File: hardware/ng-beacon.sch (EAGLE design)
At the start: 5 parts

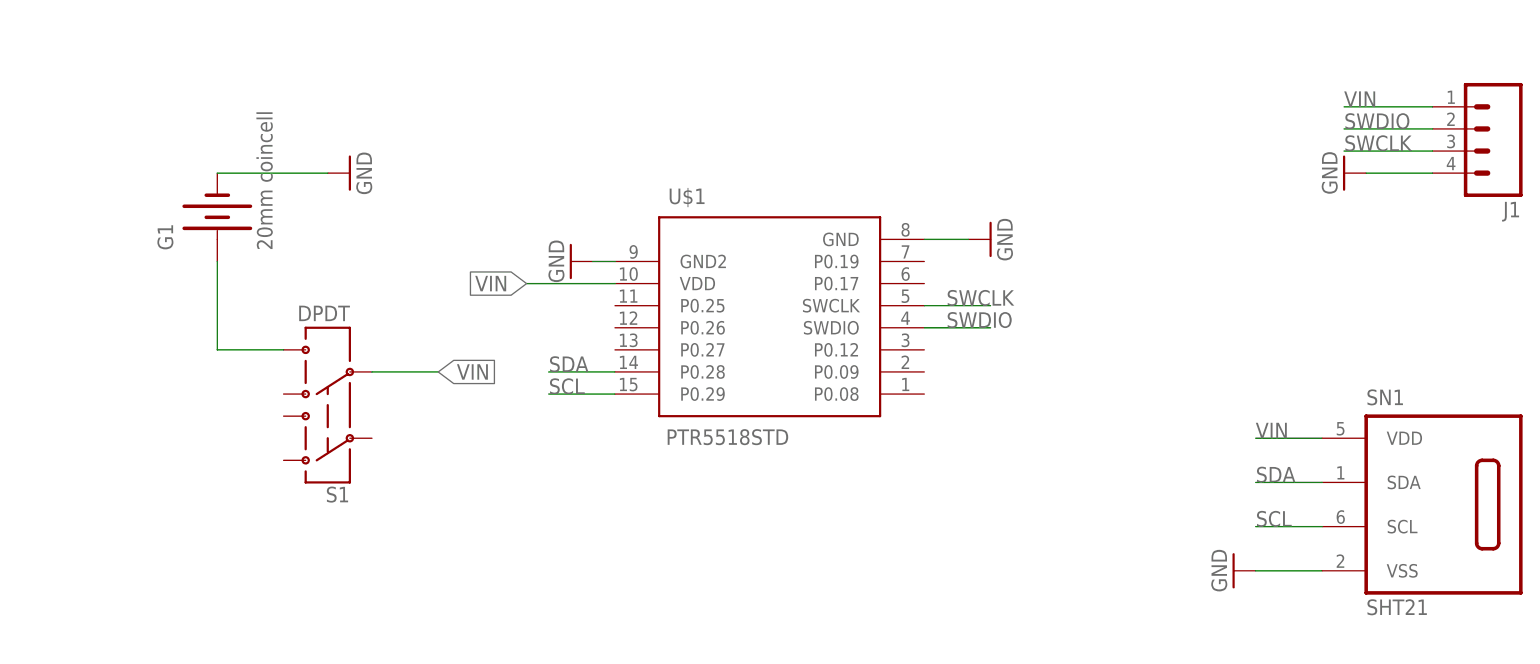
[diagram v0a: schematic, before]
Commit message: refactor: switch to MDBT42 module
nRF52, more pins and smaller footprint
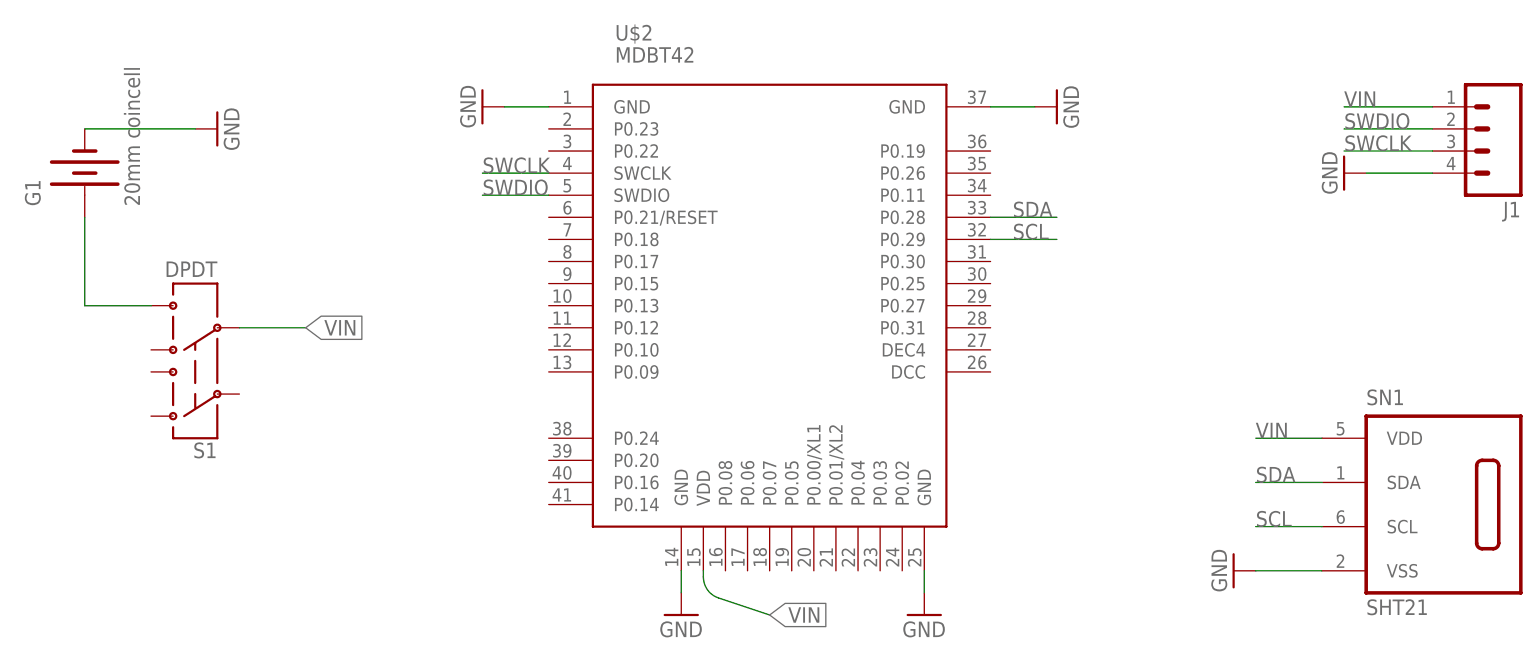
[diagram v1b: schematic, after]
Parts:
- removed U$1: PTR5518STD, PTR5518:PTR5518STD
- added U$2: MDBT42, MDBT42:MDBT42
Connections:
- net GND: now also U$2.GND@1, U$2.GND@14, U$2.GND@25, U$2.GND@37; no longer U$1.GND, U$1.GND2
- net SCL: now also U$2.P0.29; no longer U$1.P0.29
- net SDA: now also U$2.P0.28; no longer U$1.P0.28
- net SWCLK: now also U$2.SWCLK; no longer U$1.SWCLK
- net SWDIO: now also U$2.SWDIO; no longer U$1.SWDIO
- net VIN: now also U$2.VDD; no longer U$1.VDD
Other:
- moved on the sheet: G1, S1
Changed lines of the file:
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@@
 </classes>
 <parts>
-<part name="U$1" library="PTR5518" deviceset="PTR5518" device="STD"/>
 <part name="G1" library="SparkFun-Electromechanical" deviceset="BATTERY" device="20MM_4LEGS" value="20mm coincell"/>
 <part name="S1" library="SparkFun-Electromechanical" deviceset="SWITCH-DPDT" device="AYZ0202" value="DPDT"/>
 <part name="GND1" library="SparkFun-Aesthetics" deviceset="GND" device=""/>
-<part name="GND2" library="SparkFun-Aesthetics" deviceset="GND" device=""/>
 <part name="GND3" library="SparkFun-Aesthetics" deviceset="GND" device=""/>
 <part name="J1" library="SparkFun-Connectors" deviceset="M04" device="LOCK"/>
@@
 <part name="SN1" library="sensirion" deviceset="SHT21" device=""/>
 <part name="GND4" library="SparkFun-Aesthetics" deviceset="GND" device=""/>
+<part name="U$2" library="MDBT42" deviceset="MDBT42" device=""/>
+<part name="GND5" library="SparkFun-Aesthetics" deviceset="GND" device=""/>
+<part name="GND6" library="SparkFun-Aesthetics" deviceset="GND" device=""/>
+<part name="GND7" library="SparkFun-Aesthetics" deviceset="GND" device=""/>
 </parts>
 <sheets>
@@
 </plain>
 <instances>
-<instance part="U$1" gate="G$1" x="30.48" y="58.42"/>
-<instance part="G1" gate="G$1" x="-33.02" y="71.12" rot="R90"/>
-<instance part="S1" gate="G$1" x="-20.32" y="48.26" rot="R180"/>
-<instance part="GND1" gate="1" x="-17.78" y="76.2" rot="R90"/>
-<instance part="GND2" gate="1" x="55.88" y="68.58" rot="R90"/>
-<instance part="GND3" gate="1" x="7.62" y="66.04" rot="R270"/>
+<instance part="G1" gate="G$1" x="-48.26" y="76.2" rot="R90"/>
+<instance part="S1" gate="G$1" x="-35.56" y="53.34" rot="R180"/>
+<instance part="GND1" gate="1" x="-33.02" y="81.28" rot="R90"/>
+<instance part="GND3" gate="1" x="-2.54" y="83.82" rot="R270"/>
 <instance part="J1" gate="G$1" x="111.76" y="81.28" rot="R180"/>
 <instance part="GND8" gate="1" x="96.52" y="76.2" rot="R270"/>
 <instance part="SN1" gate="G$1" x="106.68" y="38.1"/>
 <instance part="GND4" gate="1" x="83.82" y="30.48" rot="R270"/>
+<instance part="U$2" gate="G$1" x="30.48" y="60.96"/>
+<instance part="GND5" gate="1" x="63.5" y="83.82" rot="R90"/>
+<instance part="GND6" gate="1" x="48.26" y="25.4"/>
+<instance part="GND7" gate="1" x="20.32" y="25.4"/>
 </instances>
 <busses>
@@
 <pinref part="GND1" gate="1" pin="GND"/>
 <pinref part="G1" gate="G$1" pin="-"/>
-<wire x1="-33.02" y1="76.2" x2="-20.32" y2="76.2" width="0.1524" layer="91"/>
-</segment>
-<segment>
-<pinref part="U$1" gate="G$1" pin="GND"/>
-<wire x1="53.34" y1="68.58" x2="48.26" y2="68.58" width="0.1524" layer="91"/>
-<pinref part="GND2" gate="1" pin="GND"/>
-</segment>
-<segment>
-<pinref part="U$1" gate="G$1" pin="GND2"/>
-<wire x1="10.16" y1="66.04" x2="12.7" y2="66.04" width="0.1524" layer="91"/>
-<pinref part="GND3" gate="1" pin="GND"/>
+<wire x1="-48.26" y1="81.28" x2="-35.56" y2="81.28" width="0.1524" layer="91"/>
 </segment>
 <segment>
@@
 <pinref part="GND4" gate="1" pin="GND"/>
 </segment>
+<segment>
+<pinref part="U$2" gate="G$1" pin="GND@1"/>
+<pinref part="GND3" gate="1" pin="GND"/>
+<wire x1="0" y1="83.82" x2="5.08" y2="83.82" width="0.1524" layer="91"/>
+</segment>
+<segment>
+<pinref part="U$2" gate="G$1" pin="GND@37"/>
+<pinref part="GND5" gate="1" pin="GND"/>
+<wire x1="55.88" y1="83.82" x2="60.96" y2="83.82" width="0.1524" layer="91"/>
+</segment>
+<segment>
+<pinref part="U$2" gate="G$1" pin="GND@25"/>
+<pinref part="GND6" gate="1" pin="GND"/>
+<wire x1="48.26" y1="30.48" x2="48.26" y2="27.94" width="0.1524" layer="91"/>
+</segment>
+<segment>
+<pinref part="U$2" gate="G$1" pin="GND@14"/>
+<pinref part="GND7" gate="1" pin="GND"/>
+<wire x1="20.32" y1="30.48" x2="20.32" y2="27.94" width="0.1524" layer="91"/>
+</segment>
 </net>
 <net name="N$1" class="0">
 <segment>
 <pinref part="G1" gate="G$1" pin="+"/>
-<wire x1="-33.02" y1="66.04" x2="-33.02" y2="55.88" width="0.1524" layer="91"/>
+<wire x1="-48.26" y1="71.12" x2="-48.26" y2="60.96" width="0.1524" layer="91"/>
 <pinref part="S1" gate="G$1" pin="6"/>
-<wire x1="-33.02" y1="55.88" x2="-25.4" y2="55.88" width="0.1524" layer="91"/>
+<wire x1="-48.26" y1="60.96" x2="-40.64" y2="60.96" width="0.1524" layer="91"/>
 </segment>
 </net>
@@
 <segment>
 <pinref part="S1" gate="G$1" pin="5"/>
-<wire x1="-15.24" y1="53.34" x2="-7.62" y2="53.34" width="0.1524" layer="91"/>
-<label x="-7.62" y="53.34" size="1.778" layer="95" xref="yes"/>
-</segment>
-<segment>
-<pinref part="U$1" gate="G$1" pin="VDD"/>
-<wire x1="12.7" y1="63.5" x2="2.54" y2="63.5" width="0.1524" layer="91"/>
-<label x="2.54" y="63.5" size="1.778" layer="95" rot="R180" xref="yes"/>
+<wire x1="-30.48" y1="58.42" x2="-22.86" y2="58.42" width="0.1524" layer="91"/>
+<label x="-22.86" y="58.42" size="1.778" layer="95" xref="yes"/>
 </segment>
 <segment>
@@
 <label x="86.36" y="45.72" size="1.778" layer="95"/>
 </segment>
+<segment>
+<pinref part="U$2" gate="G$1" pin="VDD"/>
+<wire x1="22.86" y1="30.48" x2="22.86" y2="29.770728125" width="0.1524" layer="91"/>
+<wire x1="22.86" y1="29.770728125" x2="24.59678125" y2="27.361071875" width="0.1524" layer="91" curve="71.565051"/>
+<wire x1="24.59678125" y1="27.361071875" x2="30.48" y2="25.4" width="0.1524" layer="91"/>
+<label x="30.48" y="25.4" size="1.778" layer="95" xref="yes"/>
+</segment>
 </net>
 <net name="SWCLK" class="0">
@@
 </segment>
 <segment>
-<pinref part="U$1" gate="G$1" pin="SWCLK"/>
-<wire x1="48.26" y1="60.96" x2="55.88" y2="60.96" width="0.1524" layer="91"/>
-<label x="50.8" y="60.96" size="1.778" layer="95"/>
+<pinref part="U$2" gate="G$1" pin="SWCLK"/>
+<wire x1="5.08" y1="76.2" x2="-2.54" y2="76.2" width="0.1524" layer="91"/>
+<label x="-2.54" y="76.2" size="1.778" layer="95"/>
 </segment>
 </net>
@@
 </segment>
 <segment>
-<pinref part="U$1" gate="G$1" pin="SWDIO"/>
-<wire x1="48.26" y1="58.42" x2="55.88" y2="58.42" width="0.1524" layer="91"/>
-<label x="50.8" y="58.42" size="1.778" layer="95"/>
+<pinref part="U$2" gate="G$1" pin="SWDIO"/>
+<wire x1="5.08" y1="73.66" x2="-2.54" y2="73.66" width="0.1524" layer="91"/>
+<label x="-2.54" y="73.66" size="1.778" layer="95"/>
 </segment>
 </net>
 <net name="SDA" class="0">
-<segment>
-<pinref part="U$1" gate="G$1" pin="P0.28"/>
-<wire x1="12.7" y1="53.34" x2="5.08" y2="53.34" width="0.1524" layer="91"/>
-<label x="5.08" y="53.34" size="1.778" layer="95"/>
-</segment>
 <segment>
 <pinref part="SN1" gate="G$1" pin="SDA"/>
@@
 <label x="86.36" y="40.64" size="1.778" layer="95"/>
 </segment>
+<segment>
+<pinref part="U$2" gate="G$1" pin="P0.28"/>
+<wire x1="55.88" y1="71.12" x2="63.5" y2="71.12" width="0.1524" layer="91"/>
+<label x="58.42" y="71.12" size="1.778" layer="95"/>
+</segment>
 </net>
 <net name="SCL" class="0">
-<segment>
-<pinref part="U$1" gate="G$1" pin="P0.29"/>
-<wire x1="12.7" y1="50.8" x2="5.08" y2="50.8" width="0.1524" layer="91"/>
-<label x="5.08" y="50.8" size="1.778" layer="95"/>
-</segment>
 <segment>
 <pinref part="SN1" gate="G$1" pin="SCL"/>
@@
 <label x="86.36" y="35.56" size="1.778" layer="95"/>
 </segment>
+<segment>
+<pinref part="U$2" gate="G$1" pin="P0.29"/>
+<wire x1="55.88" y1="68.58" x2="63.5" y2="68.58" width="0.1524" layer="91"/>
+<label x="58.42" y="68.58" size="1.778" layer="95"/>
+</segment>
 </net>

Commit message: add reset pads (sort of)
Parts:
- added PAD1, PAD2: (no value), wirepad:SMD2
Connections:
- new net N$4: PAD1.P, U$2.P0.17
- net GND: now also PAD2.P
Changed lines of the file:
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@@
 <part name="GND6" library="SparkFun-Aesthetics" deviceset="GND" device=""/>
 <part name="GND7" library="SparkFun-Aesthetics" deviceset="GND" device=""/>
+<part name="PAD1" library="wirepad" deviceset="SMD2" device=""/>
+<part name="PAD2" library="wirepad" deviceset="SMD2" device=""/>
+<part name="GND2" library="SparkFun-Aesthetics" deviceset="GND" device=""/>
 </parts>
 <sheets>
@@
 <instance part="GND6" gate="1" x="48.26" y="25.4"/>
 <instance part="GND7" gate="1" x="20.32" y="25.4"/>
+<instance part="PAD1" gate="1" x="-5.08" y="66.04"/>
+<instance part="PAD2" gate="1" x="-10.16" y="66.04" rot="R180"/>
+<instance part="GND2" gate="1" x="-17.78" y="66.04" rot="R270"/>
 </instances>
 <busses>
@@
 <pinref part="GND7" gate="1" pin="GND"/>
 <wire x1="20.32" y1="30.48" x2="20.32" y2="27.94" width="0.1524" layer="91"/>
+</segment>
+<segment>
+<pinref part="GND2" gate="1" pin="GND"/>
+<pinref part="PAD2" gate="1" pin="P"/>
+<wire x1="-15.24" y1="66.04" x2="-12.7" y2="66.04" width="0.1524" layer="91"/>
 </segment>
 </net>
@@
 </segment>
 </net>
+<net name="N$4" class="0">
+<segment>
+<pinref part="U$2" gate="G$1" pin="P0.17"/>
+<wire x1="5.08" y1="66.04" x2="-2.54" y2="66.04" width="0.1524" layer="91"/>
+<pinref part="PAD1" gate="1" pin="P"/>
+</segment>
+</net>
